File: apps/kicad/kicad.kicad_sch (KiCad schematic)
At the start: 7 parts, among them U1 XMC4200 (used pins), U2 LCD 16x2, U3 AHT10, U4 GPS NEO-6M, U5 POTENTIOMETER

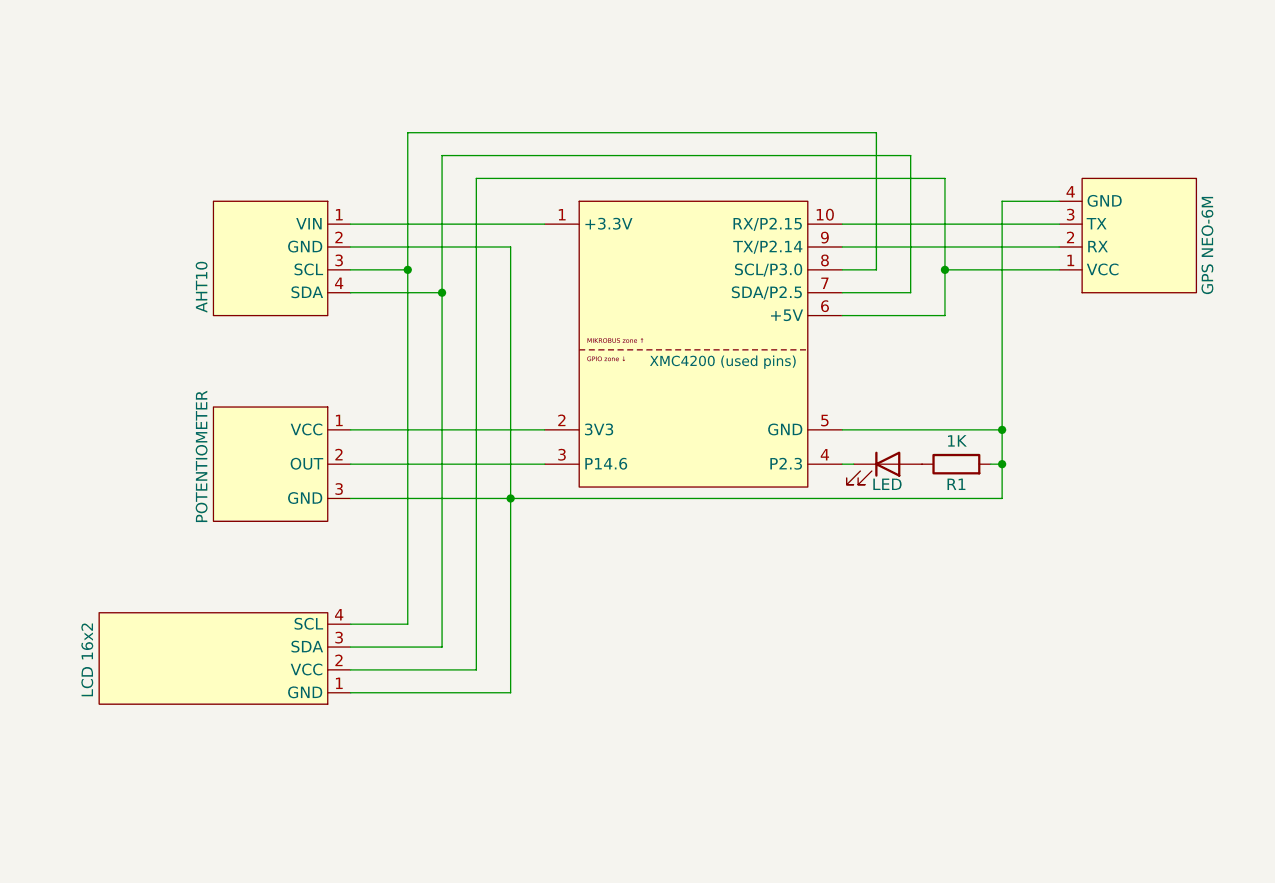
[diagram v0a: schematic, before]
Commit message: kicad: add EEPROM to schematic, regenerate outputs
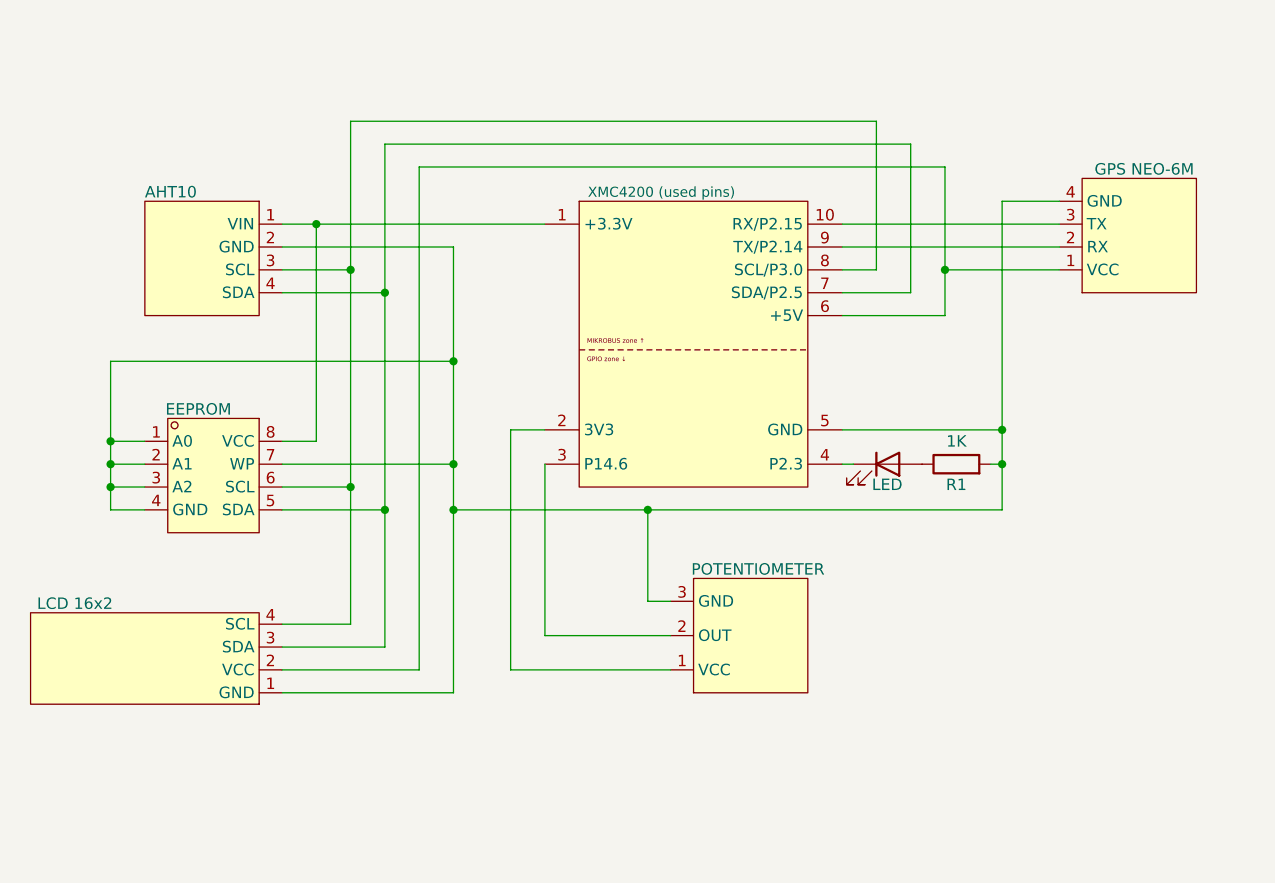
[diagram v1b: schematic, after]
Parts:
- added U6: EEPROM, symbol SISEM:AT24C32E
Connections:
- net at R1.2, U1.5 (GND), U2.1 (GND)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: now also U6.1 (A0), U6.2 (A1), U6.3 (A2), U6.4 (GND), U6.7 (WP)
- net at U1.1 (+3.3V), U3.1 (VIN): now also U6.8 (VCC)
- net at U1.7 (SDA/P2.5), U2.3 (SDA), U3.4 (SDA): now also U6.5 (SDA)
- net at U1.8 (SCL/P3.0), U2.4 (SCL), U3.3 (SCL): now also U6.6 (SCL)

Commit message: can: add GPS meta frame, gate functions on feature flags, fix short-payload padding
- gate can_send_sensor/decode_sensor behind FEATURE_AHT10; gate can_send_gps/can_send_gps_meta behind FEATURE_GPS
- rename CAN_ID_GROUP to CAN_ID_BASE; add CAN_ID_SENSOR, CAN_ID_GPS_POS, CAN_ID_GPS_META
- fix can_send() to zero-fill payloads shorter than 8 bytes via memcpy into a local buf
- send GPS metadata frame (time, satellites, fix status) on every GPGGA update
- suppress no-fix UART print unless fix is lost or satellite count changes
- pass gps_data_t struct to can_send_gps() instead of individual lat/lon floats

schematic: revise layout following good-schematic design guidelines

docs: update technical report; add kicad output README with Why/Snapshots sections and v1 snapshot
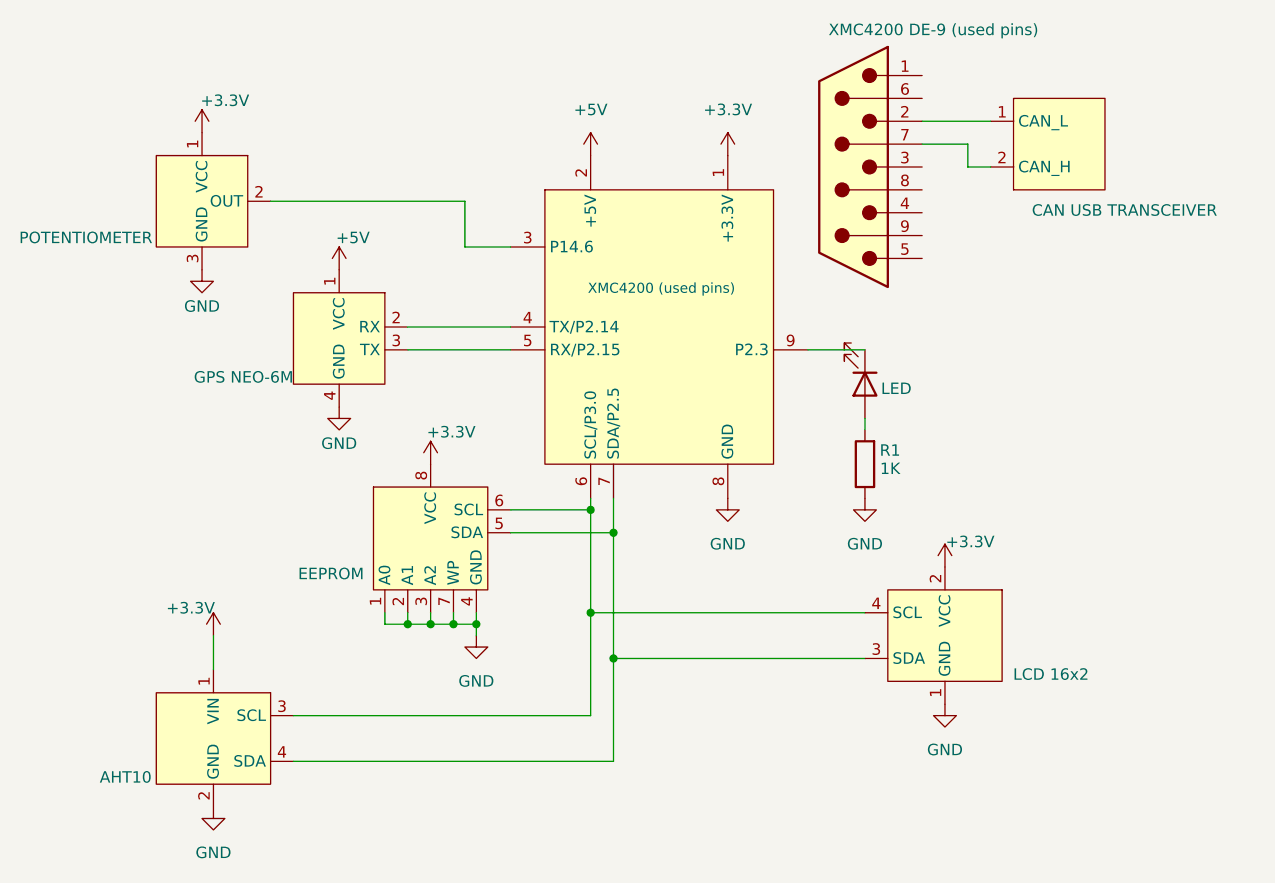
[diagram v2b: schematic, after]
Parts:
- added J1: XMC4200 DE-9 (used pins), symbol Connector:DE9_Pins
- added U7: CAN USB TRANSCEIVER, symbol SISEM:CAN_USB_TRANSCEIVER
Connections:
- net at D1.2 (A): now also R1.2; no longer R1.1
- net GND: now reaches U2.1 (GND), U3.2 (GND), U4.4 (GND), U5.3 (GND), U6.1 (A0), U6.2 (A1), U6.3 (A2), U6.4 (GND), U6.7 (WP)
- net GND: now also R1.1, U1.8 (GND); no longer R1.2, U1.5 (GND)
- net at U2.4 (SCL), U3.3 (SCL), U6.6 (SCL): now also U1.6 (SCL/P3.0); no longer U1.8 (SCL/P3.0)
- net +3.3V: now reaches U1.1 (+3.3V), U3.1 (VIN), U6.8 (VCC)
- net +3.3V: now also U2.2 (VCC), U5.1 (VCC)
- net +5V: now reaches U1.2 (+5V)
- net +5V: now also U4.1 (VCC); no longer U5.1 (VCC)
- net at U4.3 (TX): now also U1.5 (RX/P2.15); no longer U1.10 (RX/P2.15)
- net at U1.4 (TX/P2.14): now also U4.2 (RX); no longer D1.1 (K)
- net at U1.9 (P2.3): now also D1.1 (K); no longer U4.2 (RX)
- new net: J1.2, U7.1 (CAN_L)
- new net: J1.7, U7.2 (CAN_H)
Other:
- moved on the sheet: R1

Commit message: schematic change, reflect dependent files
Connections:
- net at R1.2: now also D1.1 (K); no longer D1.2 (A)
- net at U1.9 (P2.3): now also D1.2 (A); no longer D1.1 (K)
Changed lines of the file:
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@@
 	(symbol
 		(lib_id "Device:LED")
-		(at 132.08 106.68 270)
+		(at 132.08 106.68 90)
 		(unit 1)
 		(body_style 1)
@@
 		(dnp no)
 		(property "Reference" "D1"
-			(at 138.43 105.0925 0)
+			(at 125.73 108.2675 0)
 			(hide yes)
 			(show_name no)
@@
 		)
 		(property "Value" "LED"
-			(at 133.858 107.188 90)
+			(at 137.414 106.68 90)
 			(show_name no)
 			(do_not_autoplace no)
